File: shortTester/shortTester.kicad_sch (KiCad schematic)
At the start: 5 parts, among them J2 Conn_02x38_Counter_Clockwise, U2 Pico

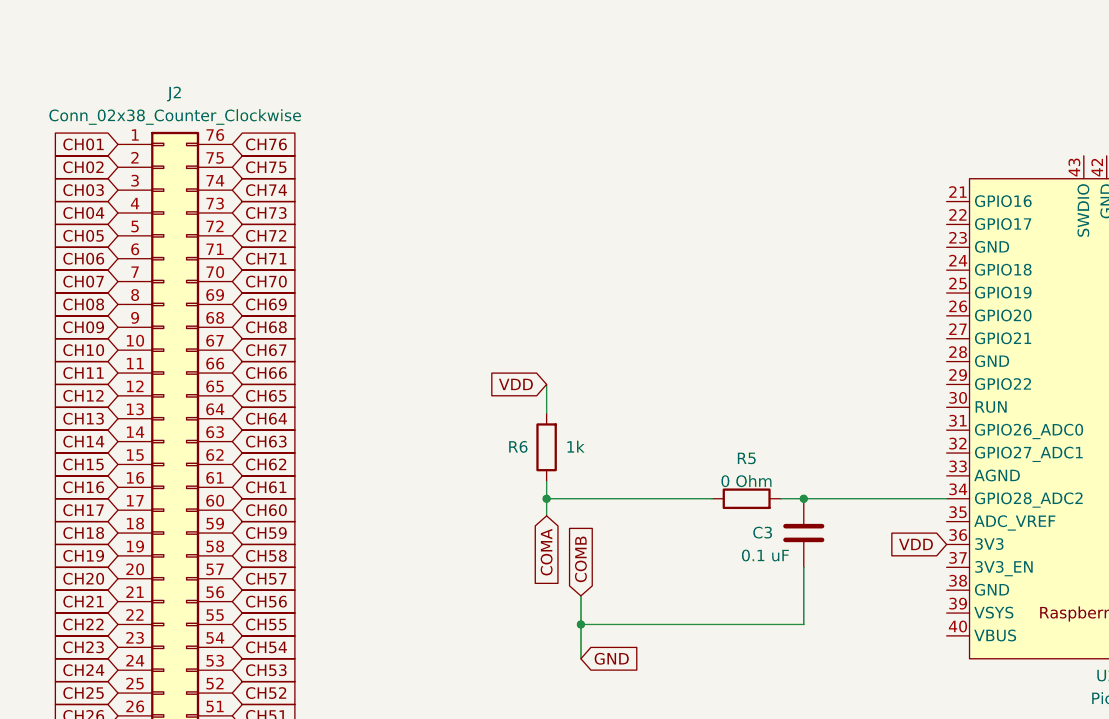
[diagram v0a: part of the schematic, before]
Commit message: Fixed missing tracks. Simplified MUx GND. Added software.
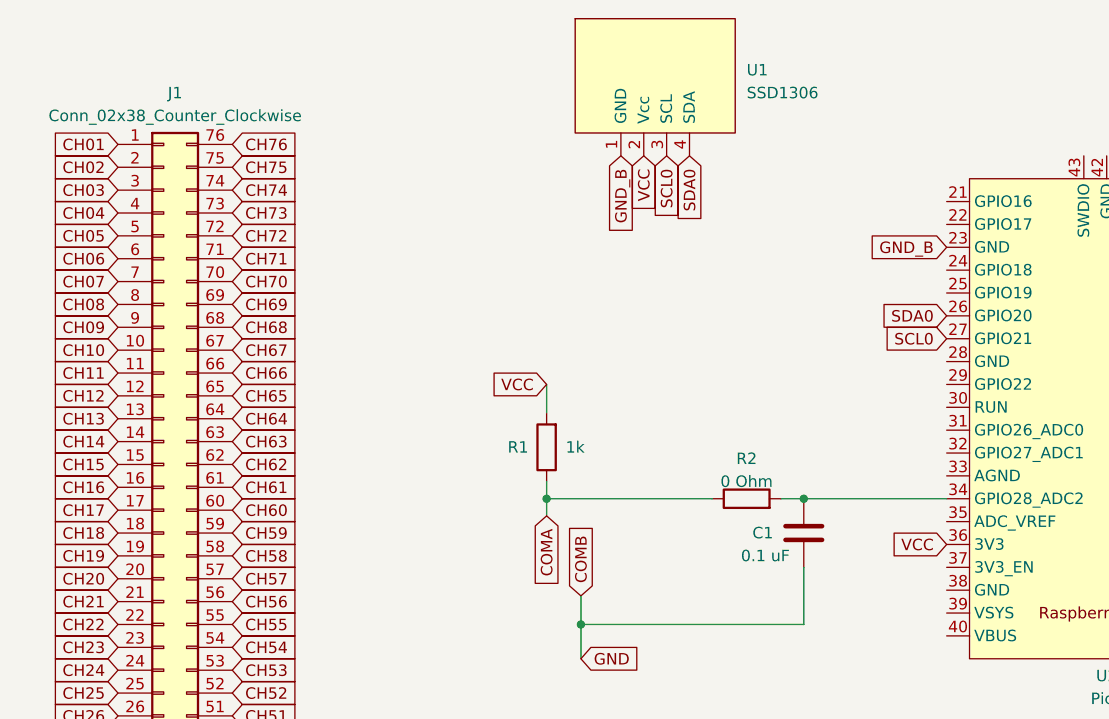
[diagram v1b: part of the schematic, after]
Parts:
- added U1: SSD1306, skLib:SSD1306, symbol skLib:SSD1306
- renumbered C3 to C1, J2 to J1, R6 to R1, R5 to R2
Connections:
- net GND_B: now reaches U2.23 (GND)
- net GND_B: now also U1.1 (GND)
- net SDA0: now reaches U2.26 (GPIO20)
- net SDA0: now also U1.4 (SDA)
- net SCL0: now reaches U2.27 (GPIO21)
- net SCL0: now also U1.3 (SCL)
- net VDD renamed VCC
- net VCC: now also U1.2 (Vcc)
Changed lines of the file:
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@@
+    )
+  )
+  (global_label "GND_B" (shape input) (at 165.1 41.275 270) (fields_autoplaced)
+    (effects (font (size 1.27 1.27)) (justify right))
+    (property "Intersheetrefs" "${INTERSHEET_REFS}" (at 165.1 50.2889 90)
+      (effects (font (size 1.27 1.27)) (justify right) hide)
     )
   )
@@
     )
   )
+  (global_label "SCL0" (shape input) (at 170.18 41.275 270) (fields_autoplaced)
+    (effects (font (size 1.27 1.27)) (justify right))
+    (property "Intersheetrefs" "${INTERSHEET_REFS}" (at 170.18 48.8979 90)
+      (effects (font (size 1.27 1.27)) (justify right) hide)
+    )
+  )
   (global_label "CH20" (shape input) (at 109.22 88.265 180) (fields_autoplaced)
     (effects (font (size 1.27 1.27)) (justify right))
@@
     )
   )
+  (global_label "VCC" (shape input) (at 167.64 41.275 270) (fields_autoplaced)
+    (effects (font (size 1.27 1.27)) (justify right))
+    (property "Intersheetrefs" "${INTERSHEET_REFS}" (at 167.64 47.8094 90)
+      (effects (font (size 1.27 1.27)) (justify right) hide)
+    )
+  )
   (global_label "CH16" (shape input) (at 109.22 78.105 180) (fields_autoplaced)
     (effects (font (size 1.27 1.27)) (justify right))
@@
     )
   )
-  (global_label "VDD" (shape input) (at 201.295 84.455 180) (fields_autoplaced)
+  (global_label "VCC" (shape input) (at 201.295 84.455 180) (fields_autoplaced)
     (effects (font (size 1.27 1.27)) (justify right))
     (property "Intersheetrefs" "${INTERSHEET_REFS}" (at 194.7606 84.455 0)
@@
     )
   )
+  (global_label "SDA0" (shape input) (at 172.72 41.275 270) (fields_autoplaced)
+    (effects (font (size 1.27 1.27)) (justify right))
+    (property "Intersheetrefs" "${INTERSHEET_REFS}" (at 172.72 48.9584 90)
+      (effects (font (size 1.27 1.27)) (justify right) hide)
+    )
+  )
   (global_label "CH62" (shape input) (at 121.92 75.565 0) (fields_autoplaced)
     (effects (font (size 1.27 1.27)) (justify left))
@@
     )
   )
+  (global_label "SCL0" (shape input) (at 201.295 61.595 180) (fields_autoplaced)
+    (effects (font (size 1.27 1.27)) (justify right))
+    (property "Intersheetrefs" "${INTERSHEET_REFS}" (at 193.6721 61.595 0)
+      (effects (font (size 1.27 1.27)) (justify right) hide)
+    )
+  )
   (global_label "SA11" (shape input) (at 236.855 92.075 0) (fields_autoplaced)
     (effects (font (size 1.27 1.27)) (justify left))
@@
     )
   )
-  (global_label "VDD" (shape input) (at 156.845 66.675 180) (fields_autoplaced)
+  (global_label "VCC" (shape input) (at 156.845 66.675 180) (fields_autoplaced)
     (effects (font (size 1.27 1.27)) (justify right))
     (property "Intersheetrefs" "${INTERSHEET_REFS}" (at 150.3106 66.675 0)
@@
     )
   )
+  (global_label "SDA0" (shape input) (at 201.295 59.055 180) (fields_autoplaced)
+    (effects (font (size 1.27 1.27)) (justify right))
+    (property "Intersheetrefs" "${INTERSHEET_REFS}" (at 193.6116 59.055 0)
+      (effects (font (size 1.27 1.27)) (justify right) hide)
+    )
+  )
   (global_label "SA22" (shape input) (at 236.855 74.295 0) (fields_autoplaced)
     (effects (font (size 1.27 1.27)) (justify left))
@@
     (effects (font (size 1.27 1.27)) (justify right))
     (property "Intersheetrefs" "${INTERSHEET_REFS}" (at 101.2947 40.005 0)
+      (effects (font (size 1.27 1.27)) (justify right) hide)
+    )
+  )
+  (global_label "GND_B" (shape input) (at 201.295 51.435 180) (fields_autoplaced)
+    (effects (font (size 1.27 1.27)) (justify right))
+    (property "Intersheetrefs" "${INTERSHEET_REFS}" (at 192.2811 51.435 0)
       (effects (font (size 1.27 1.27)) (justify right) hide)
     )
@@
   (symbol (lib_id "Device:R") (at 156.845 73.66 180) (unit 1)
     (in_bom yes) (on_board yes) (dnp no)
-    (property "Reference" "R6" (at 153.67 73.66 0)
+    (property "Reference" "R1" (at 153.67 73.66 0)
       (effects (font (size 1.27 1.27)))
     )
@@
       (project "shortTester"
         (path "/437377eb-9519-4c2d-a62b-5828634d2eb4"
-          (reference "R6") (unit 1)
+          (reference "R1") (unit 1)
+        )
+      )
+    )
+  )
+  (symbol (lib_id "skLib:SSD1306") (at 168.91 32.385 0) (unit 1)
+    (in_bom yes) (on_board yes) (dnp no) (fields_autoplaced)
+    (property "Reference" "U1" (at 179.07 31.75 0)
+      (effects (font (size 1.27 1.27)) (justify left))
+    )
+    (property "Value" "SSD1306" (at 179.07 34.29 0)
+      (effects (font (size 1.27 1.27)) (justify left))
+    )
+    (property "Footprint" "skLib:SSD1306" (at 168.91 24.765 0)
+      (effects (font (size 1.27 1.27)) hide)
+    )
+    (property "Datasheet" "" (at 168.91 24.765 0)
+      (effects (font (size 1.27 1.27)) hide)
+    )
+    (pin "1")
+    (pin "2")
+    (pin "3")
+    (pin "4")
+    (instances
+      (project "shortTester"
+        (path "/437377eb-9519-4c2d-a62b-5828634d2eb4"
+          (reference "U1") (unit 1)
         )
       )
@@
   (symbol (lib_id "Device:R") (at 179.07 79.375 90) (unit 1)
     (in_bom yes) (on_board yes) (dnp no) (fields_autoplaced)
-    (property "Reference" "R5" (at 179.07 74.93 90)
+    (property "Reference" "R2" (at 179.07 74.93 90)
       (effects (font (size 1.27 1.27)))
     )
@@
       (project "shortTester"
         (path "/437377eb-9519-4c2d-a62b-5828634d2eb4"
-          (reference "R5") (unit 1)
+          (reference "R2") (unit 1)
         )
       )
@@
   (symbol (lib_id "Connector_Generic:Conn_02x38_Counter_Clockwise") (at 114.3 85.725 0) (unit 1)
     (in_bom yes) (on_board yes) (dnp no) (fields_autoplaced)
-    (property "Reference" "J2" (at 115.57 34.29 0)
+    (property "Reference" "J1" (at 115.57 34.29 0)
       (effects (font (size 1.27 1.27)))
     )
@@
       (project "shortTester"
         (path "/437377eb-9519-4c2d-a62b-5828634d2eb4"
-          (reference "J2") (unit 1)
+          (reference "J1") (unit 1)
         )
       )
@@
   (symbol (lib_id "Device:C") (at 185.42 83.185 0) (unit 1)
     (in_bom yes) (on_board yes) (dnp no)
-    (property "Reference" "C3" (at 179.705 83.185 0)
+    (property "Reference" "C1" (at 179.705 83.185 0)
       (effects (font (size 1.27 1.27)) (justify left))
     )
@@
       (project "shortTester"
         (path "/437377eb-9519-4c2d-a62b-5828634d2eb4"
-          (reference "C3") (unit 1)
+          (reference "C1") (unit 1)
         )
       )
